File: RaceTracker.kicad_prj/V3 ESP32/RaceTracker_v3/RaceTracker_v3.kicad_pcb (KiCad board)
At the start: 2 copper layers, 70 x 97 mm, 39 parts, among them J1 USB-C, J2 Battery, J3 Qwiic GPS (I2C), J4 microSD, J5 UART Debug, SW1 PWR, SW2 RESET, SW3 BOOT, U1 ESP32-S3-WROOM-1-N8, U2 MCP73831T-2ACI/OT, U3 AP2112K-3.3

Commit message: V3: C2 (MCP73831 VDD-Entkopplung) von 1uF auf 4.7uF korrigiert
Datenblatt-Review aller Bauteile gegen die jeweilige typische Beschaltung
(MCP73831, AP2112K-3.3, USBLC6-2SC6, PESD5V0S1UL real heruntergeladen und
gegengeprueft). Einziger echter Fund: MCP73831 Abschnitt 3.1 verlangt am
VDD-Pin explizit "Bypass to VSS with a minimum of 4.7 uF" -- C2 hatte nur
1uF. VBAT-seitige Entkopplung (C3=4.7uF) stimmte bereits exakt. AP2112K-3.3
(1uF/1uF), USBLC6-2SC6 (keine externen Bauteile noetig) und PESD5V0S1UL
(Polaritaet K->VBUS, A->GND) bestaetigt korrekt.

ERC 0/0, DRC 0 Fehler nach dem Fix weiterhin bestaetigt.
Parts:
- C2: value 1uF -> 4.7uF

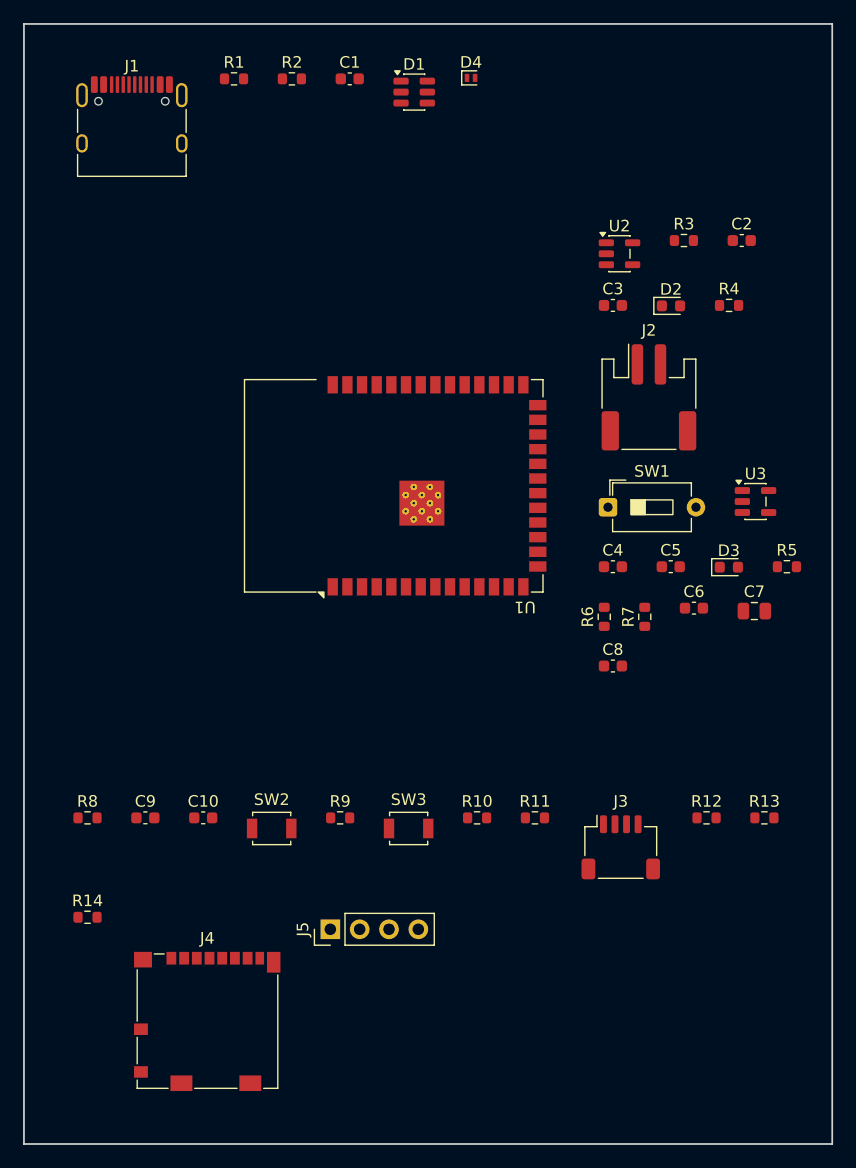
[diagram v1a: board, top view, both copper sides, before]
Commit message: V3 PCB: manuelle Platzierung des Nutzers uebernommen, 6 DRC-Fehler behoben
Nutzer hat Bauteile in der KiCad-GUI manuell verschoben (deutlich
kompakteres Layout als mein Original) und im alten "New Version with
WROOM"-Pfad gespeichert (KiCad hatte die Datei wohl noch von vor der
Umbenennung offen). Fehler wurden dort chirurgisch behoben (pcbnew
LoadBoard + gezielte Korrektur, nicht neu generiert -- bewahrt die
manuelle Platzierung vollstaendig):

- copper_edge_clearance: R14-Pad war 0.45mm statt min. 0.5mm vom
  Rand entfernt -- Bauteil um 0.15mm verschoben.
- 4x Silkscreen-Warnungen (J1/D2/SW1-Referenzfeld ueberlappte mit
  Board-Rand, U1-Referenzfeld oder U1-Pads) -- nur die Textfelder neu
  positioniert, keine Bauteile bewegt.

kicad-cli pcb drc: 0 Fehler. Ergebnis nach RaceTracker_v3/ synchronisiert
(dort ist jetzt die massgebliche, aktuelle Version) und den verwaisten
alten Ordner geloescht.
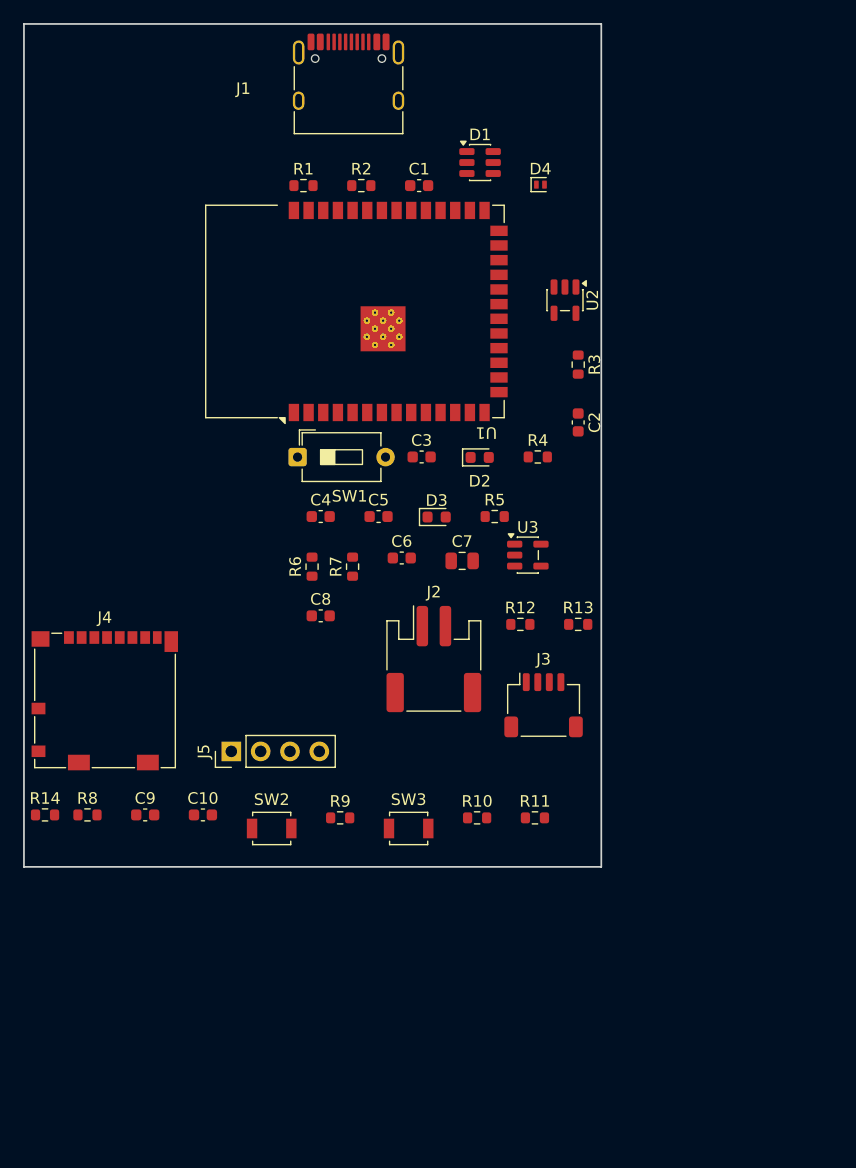
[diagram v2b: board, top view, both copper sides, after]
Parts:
- C2: value 4.7uF -> 1uF
- moved J2 29.3 mm to (35.5, 55.0)
- moved J4 29.2 mm to (7.00, 58.6)
- moved SW1 27.2 mm to (23.7, 37.5)
- moved C4 25.7 mm to (25.7, 42.7)
- moved C8 25.7 mm to (25.7, 51.3)
- moved R6 25.7 mm to (24.9, 47.0)
- moved C5 25.7 mm to (30.7, 42.7)
- moved C6 25.7 mm to (32.7, 46.2)
- moved C7 25.7 mm to (38.0, 46.5)
- moved D3 25.7 mm to (35.7, 42.7)
- moved R5 25.7 mm to (40.8, 42.7)
- moved R7 25.7 mm to (28.5, 47.0)
- moved R12 23.3 mm to (43.0, 52.0)
- moved R13 23.3 mm to (48.0, 52.0)
- moved C2 21.2 mm to (48.0, 34.5), turned to -90 degrees
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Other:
- board size 70 x 97 mm -> 50 x 73 mm
